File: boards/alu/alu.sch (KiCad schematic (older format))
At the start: 80 parts, among them U1 28C256, U2 74ACT08, U3 28C256, U4 74ACT00, U5 74ACT02

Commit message: PLCC-32 socket footprint
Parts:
- removed U1, U3: 28C256, Package_LCC:PLCC-28_SMD-Socket, symbol Memory_EEPROM:28C256
- added U1, U3: AT28C256-PLCC32, missing:PLCC-32_SMD_Socket, symbol missing:AT28C256-PLCC32
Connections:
- net GND: now also U1.16 (GND), U1.23 (~CE), U3.16 (GND), U3.23 (~CE)
- net VCC: now also U1.31 (~WE), U1.32 (VCC), U3.31 (~WE), U3.32 (VCC)
- net a0: now also U1.11 (A0)
- net a1: now also U1.10 (A1)
- net a2: now also U1.9 (A2)
- net a3: now also U1.8 (A3)
- net a4: now also U3.11 (A0)
- net a5: now also U3.10 (A1)
- net a6: now also U3.9 (A2)
- net a7: now also U3.8 (A3)
- net b0: now also U1.7 (A4)
- net b1: now also U1.6 (A5)
- net b2: now also U1.5 (A6)
- net b3: now also U1.4 (A7)
- net b4: now also U3.7 (A4)
- net b5: now also U3.6 (A5)
- net b6: now also U3.5 (A6)
- net b7: now also U3.4 (A7)
- net carry_in: now also U1.3 (A12), U3.3 (A12)
- net flags2: now also U3.18 (IO3)
- net flags3: now also U3.21 (IO6)
- net from_hi: now also U1.30 (A13)
- net from_lo: now also U3.30 (A13)
- net invert: now also U1.2 (A14), U3.2 (A14)
- net op0: now also U1.29 (A8), U3.29 (A8)
- net op1: now also U1.28 (A9), U3.28 (A9)
- net op2: now also U1.24 (A10), U3.24 (A10)
- net op3: now also U1.27 (A11), U3.27 (A11)
- net r0: now also U1.13 (IO0)
- net r1: now also U1.14 (IO1)
- net r2: now also U1.15 (IO2)
- net r3: now also U1.18 (IO3)
- net r4: now also U3.13 (IO0)
- net r5: now also U3.14 (IO1)
- net r6: now also U3.15 (IO2)
- net to_hi: now also U1.20 (IO5)
- net to_lo: now also U3.20 (IO5)
- net ~carry_hi: now also U3.19 (IO4)
- net ~carry_lo: now also U1.19 (IO4)
- net ~oe: now also U1.25 (~OE), U3.25 (~OE)
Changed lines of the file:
@@
 Comment4 ""
 $EndDescr
-$Comp
-L Memory_EEPROM:28C256 U1
-U 1 1 5FC22E82
-P 6500 3650
-F 0 "U1" H 6900 2700 50  0000 C CNN
-F 1 "28C256" H 6850 2550 50  0000 C CNN
-F 2 "Package_LCC:PLCC-28_SMD-Socket" H 6500 3650 50  0001 C CNN
-F 3 "http://ww1.microchip.com/downloads/en/DeviceDoc/doc0006.pdf" H 6500 3650 50  0001 C CNN
-	1    6500 3650
-	1    0    0    -1
-$EndComp
 Text Label 6100 2750 2    50   ~ 0
 a0
@@
 Text Label 8700 3250 0    50   ~ 0
 to_lo
-$Comp
-L Memory_EEPROM:28C256 U3
-U 1 1 5FC23A8E
-P 8300 3650
-F 0 "U3" H 8700 2700 50  0000 C CNN
-F 1 "28C256" H 8700 2550 50  0000 C CNN
-F 2 "Package_LCC:PLCC-28_SMD-Socket" H 8300 3650 50  0001 C CNN
-F 3 "http://ww1.microchip.com/downloads/en/DeviceDoc/doc0006.pdf" H 8300 3650 50  0001 C CNN
-	1    8300 3650
-	1    0    0    -1
-$EndComp
 NoConn ~ 8700 3450
 $Comp
@@
 L power:VCC #PWR01
 U 1 1 5FC2D9E5
-P 6100 4350
-F 0 "#PWR01" H 6100 4200 50  0001 C CNN
-F 1 "VCC" V 6118 4477 50  0000 L CNN
-F 2 "" H 6100 4350 50  0001 C CNN
-F 3 "" H 6100 4350 50  0001 C CNN
-	1    6100 4350
+P 6100 4450
+F 0 "#PWR01" H 6100 4300 50  0001 C CNN
+F 1 "VCC" V 6118 4577 50  0000 L CNN
+F 2 "" H 6100 4450 50  0001 C CNN
+F 3 "" H 6100 4450 50  0001 C CNN
+	1    6100 4450
 	0    -1   -1   0
 $EndComp
@@
 L power:VCC #PWR07
 U 1 1 5FC2E2AC
-P 7900 4350
-F 0 "#PWR07" H 7900 4200 50  0001 C CNN
-F 1 "VCC" V 7918 4477 50  0000 L CNN
-F 2 "" H 7900 4350 50  0001 C CNN
-F 3 "" H 7900 4350 50  0001 C CNN
-	1    7900 4350
+P 7900 4450
+F 0 "#PWR07" H 7900 4300 50  0001 C CNN
+F 1 "VCC" V 7918 4577 50  0000 L CNN
+F 2 "" H 7900 4450 50  0001 C CNN
+F 3 "" H 7900 4450 50  0001 C CNN
+	1    7900 4450
 	0    -1   -1   0
 $EndComp
@@
 Text Label 12950 3100 0    50   ~ 0
 flags[0..3]
-Text Label 7900 4450 2    50   ~ 0
+Text Label 7900 4350 2    50   ~ 0
 ~oe
-Text Label 6100 4450 2    50   ~ 0
+Text Label 6100 4350 2    50   ~ 0
 ~oe
 Text Label 9350 3650 0    50   ~ 0
@@
 Wire Bus Line
 	10750 1700 10750 3100
+$Comp
+L missing:AT28C256-PLCC32 U1
+U 1 1 60197966
+P 6500 3650
+F 0 "U1" H 6500 4931 50  0000 C CNN
+F 1 "AT28C256-PLCC32" H 6500 4840 50  0000 C CNN
+F 2 "missing:PLCC-32_SMD_Socket" H 6750 4000 50  0001 C CNN
+F 3 "http://ww1.microchip.com/downloads/en/DeviceDoc/doc0006.pdf" H 6750 4000 50  0001 C CNN
+	1    6500 3650
+	1    0    0    -1
+$EndComp
+$Comp
+L missing:AT28C256-PLCC32 U3
+U 1 1 60199147
+P 8300 3650
+F 0 "U3" H 8300 4931 50  0000 C CNN
+F 1 "AT28C256-PLCC32" H 8300 4840 50  0000 C CNN
+F 2 "missing:PLCC-32_SMD_Socket" H 8550 4000 50  0001 C CNN
+F 3 "http://ww1.microchip.com/downloads/en/DeviceDoc/doc0006.pdf" H 8550 4000 50  0001 C CNN
+	1    8300 3650
+	1    0    0    -1
+$EndComp
 $EndSCHEMATC

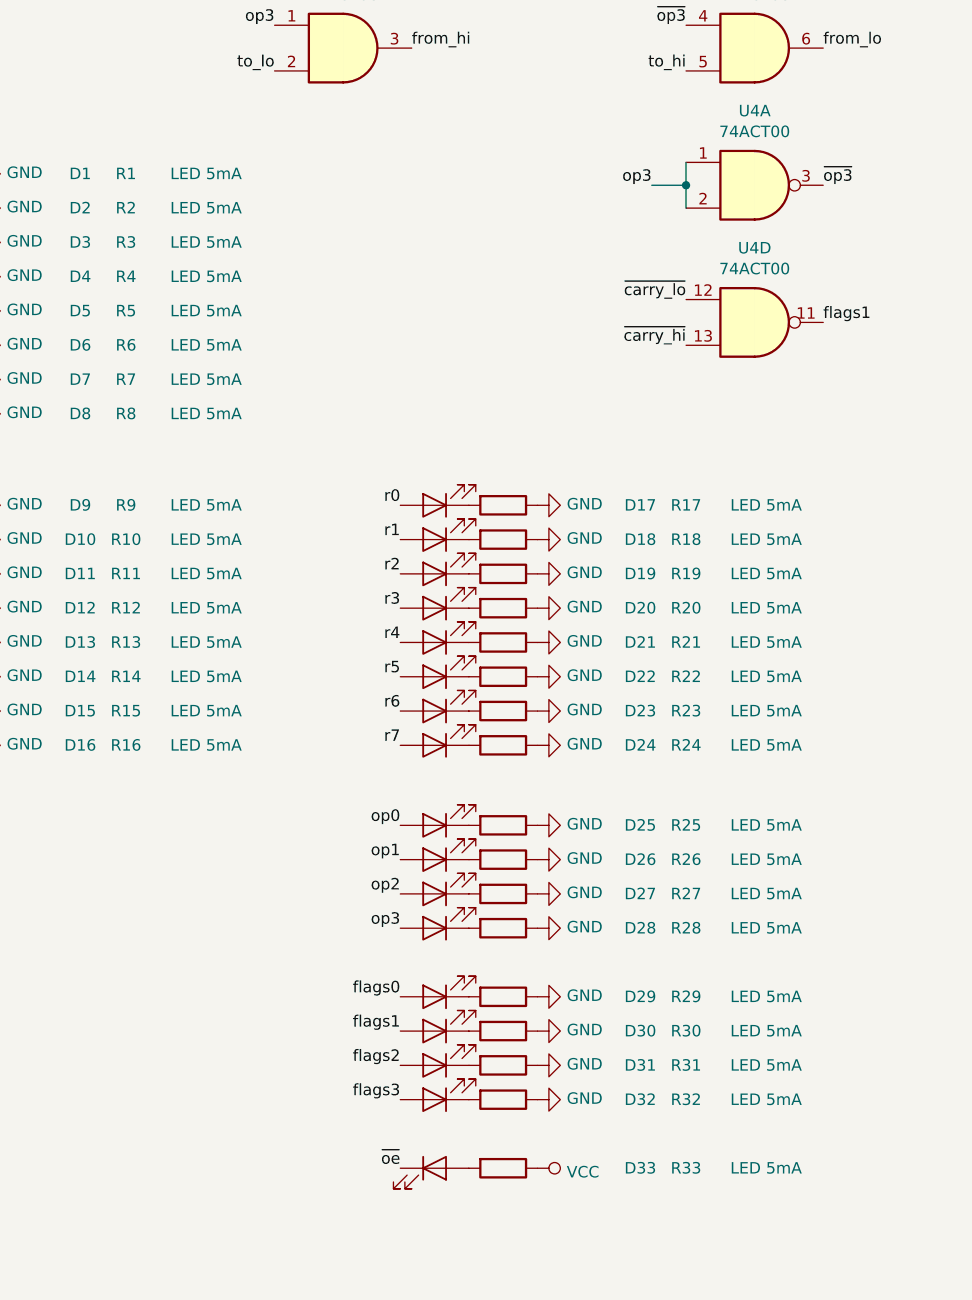
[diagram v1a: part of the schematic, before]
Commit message: LEDs and LED resistors
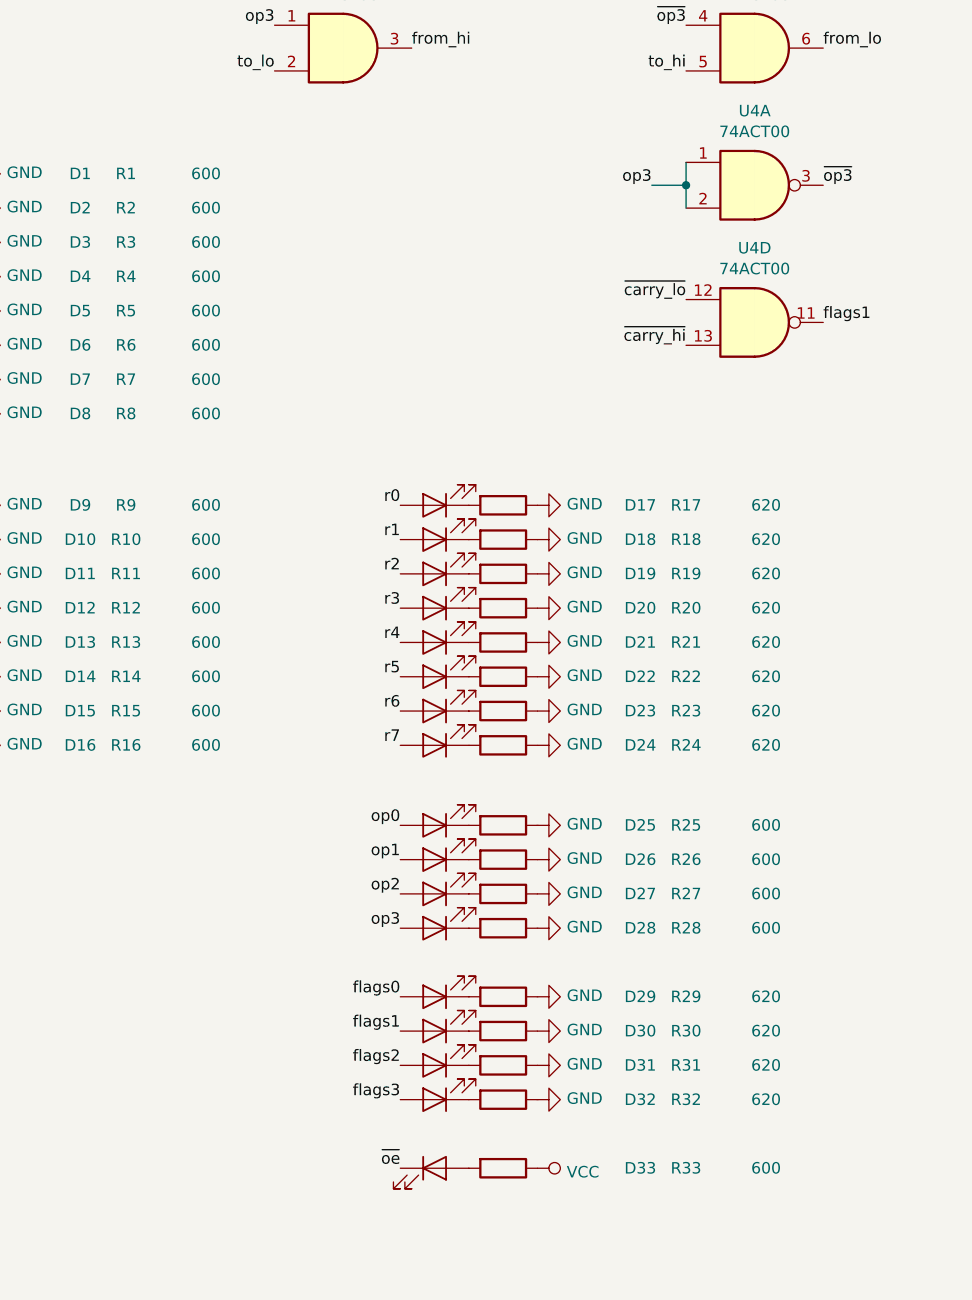
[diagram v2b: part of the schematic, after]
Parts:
- D1, D10, D11, D12, D13, D14, D15, D16, D2, D25, D26, D27, D28, D3, D33, D4, D5, D6, D7, D8, D9: value LED -> KP-2012CGCK
- D17, D18, D19, D20, D21, D22, D23, D24, D29, D30, D31, D32: value LED -> KP-2012EC
- R1, R10, R11, R12, R13, R14, R15, R16, R2, R25, R26, R27, R28, R3, R33, R4, R5, R6, R7, R8, R9: value LED 5mA -> 600
- R17, R18, R19, R20, R21, R22, R23, R24, R29, R30, R31, R32: value LED 5mA -> 620

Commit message: Part names
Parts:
- U2: value 74ACT08 -> SN74ACT08PW
- U4: value 74ACT00 -> 74ACT00MTCX; footprint Package_SO:SOIC-14_3.9x8.7mm_P1.27mm -> Package_SO:TSSOP-14_4.4x5mm_P0.65mm
- U5: value 74ACT02 -> MC74ACT02DTR2G
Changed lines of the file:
@@
 P 6500 5500
 F 0 "U2" H 6500 5825 50  0000 C CNN
-F 1 "74ACT08" H 6500 5734 50  0000 C CNN
+F 1 "SN74ACT08PW" H 6500 5734 50  0000 C CNN
 F 2 "Package_SO:TSSOP-14_4.4x5mm_P0.65mm" H 6500 5500 50  0001 C CNN
 F 3 "http://www.ti.com/lit/gpn/sn74LS08" H 6500 5500 50  0001 C CNN
@@
 P 8300 5500
 F 0 "U2" H 8300 5825 50  0000 C CNN
-F 1 "74ACT08" H 8300 5734 50  0000 C CNN
+F 1 "SN74ACT08PW" H 8300 5734 50  0000 C CNN
 F 2 "Package_SO:TSSOP-14_4.4x5mm_P0.65mm" H 8300 5500 50  0001 C CNN
 F 3 "http://www.ti.com/lit/gpn/sn74LS08" H 8300 5500 50  0001 C CNN
@@
 P 10100 5750
 F 0 "U5" H 10100 6075 50  0000 C CNN
-F 1 "74ACT02" H 10100 5984 50  0000 C CNN
+F 1 "MC74ACT02DTR2G" H 10100 5984 50  0000 C CNN
 F 2 "Package_SO:TSSOP-14_4.4x5mm_P0.65mm" H 10100 5750 50  0001 C CNN
 F 3 "http://www.ti.com/lit/gpn/sn74ls02" H 10100 5750 50  0001 C CNN
@@
 P 10100 6300
 F 0 "U5" H 10100 6625 50  0000 C CNN
-F 1 "74ACT02" H 10100 6534 50  0000 C CNN
+F 1 "MC74ACT02DTR2G" H 10100 6534 50  0000 C CNN
 F 2 "Package_SO:TSSOP-14_4.4x5mm_P0.65mm" H 10100 6300 50  0001 C CNN
 F 3 "http://www.ti.com/lit/gpn/sn74ls02" H 10100 6300 50  0001 C CNN
@@
 P 10100 6850
 F 0 "U5" H 10100 7175 50  0000 C CNN
-F 1 "74ACT02" H 10100 7084 50  0000 C CNN
+F 1 "MC74ACT02DTR2G" H 10100 7084 50  0000 C CNN
 F 2 "Package_SO:TSSOP-14_4.4x5mm_P0.65mm" H 10100 6850 50  0001 C CNN
 F 3 "http://www.ti.com/lit/gpn/sn74ls02" H 10100 6850 50  0001 C CNN
@@
 P 10100 7400
 F 0 "U5" H 10100 7725 50  0000 C CNN
-F 1 "74ACT02" H 10100 7634 50  0000 C CNN
+F 1 "MC74ACT02DTR2G" H 10100 7634 50  0000 C CNN
 F 2 "Package_SO:TSSOP-14_4.4x5mm_P0.65mm" H 10100 7400 50  0001 C CNN
 F 3 "http://www.ti.com/lit/gpn/sn74ls02" H 10100 7400 50  0001 C CNN
@@
 P 11050 6050
 F 0 "U2" H 11050 6375 50  0000 C CNN
-F 1 "74ACT08" H 11050 6284 50  0000 C CNN
+F 1 "SN74ACT08PW" H 11050 6284 50  0000 C CNN
 F 2 "Package_SO:TSSOP-14_4.4x5mm_P0.65mm" H 11050 6050 50  0001 C CNN
 F 3 "http://www.ti.com/lit/gpn/sn74LS08" H 11050 6050 50  0001 C CNN
@@
 P 11050 7100
 F 0 "U2" H 11050 7425 50  0000 C CNN
-F 1 "74ACT08" H 11050 7334 50  0000 C CNN
+F 1 "SN74ACT08PW" H 11050 7334 50  0000 C CNN
 F 2 "Package_SO:TSSOP-14_4.4x5mm_P0.65mm" H 11050 7100 50  0001 C CNN
 F 3 "http://www.ti.com/lit/gpn/sn74LS08" H 11050 7100 50  0001 C CNN
@@
 P 13500 8900
 F 0 "U2" H 13730 8946 50  0000 L CNN
-F 1 "74ACT08" H 13730 8855 50  0000 L CNN
+F 1 "SN74ACT08PW" H 13730 8855 50  0000 L CNN
 F 2 "Package_SO:TSSOP-14_4.4x5mm_P0.65mm" H 13500 8900 50  0001 C CNN
 F 3 "http://www.ti.com/lit/gpn/sn74LS08" H 13500 8900 50  0001 C CNN
@@
 P 14350 8900
 F 0 "U5" H 14580 8946 50  0000 L CNN
-F 1 "74ACT02" H 14580 8855 50  0000 L CNN
+F 1 "MC74ACT02DTR2G" H 14580 8855 50  0000 L CNN
 F 2 "Package_SO:TSSOP-14_4.4x5mm_P0.65mm" H 14350 8900 50  0001 C CNN
 F 3 "http://www.ti.com/lit/gpn/sn74ls02" H 14350 8900 50  0001 C CNN
@@
 P 8300 6100
 F 0 "U4" H 8300 6425 50  0000 C CNN
-F 1 "74ACT00" H 8300 6334 50  0000 C CNN
-F 2 "Package_SO:SOIC-14_3.9x8.7mm_P1.27mm" H 8300 6100 50  0001 C CNN
+F 1 "74ACT00MTCX" H 8300 6334 50  0000 C CNN
+F 2 "Package_SO:TSSOP-14_4.4x5mm_P0.65mm" H 8300 6100 50  0001 C CNN
 F 3 "http://www.ti.com/lit/gpn/sn74hc00" H 8300 6100 50  0001 C CNN
 	1    8300 6100
@@
 P 11900 6550
 F 0 "U4" H 11900 6875 50  0000 C CNN
-F 1 "74ACT00" H 11900 6784 50  0000 C CNN
-F 2 "Package_SO:SOIC-14_3.9x8.7mm_P1.27mm" H 11900 6550 50  0001 C CNN
+F 1 "74ACT00MTCX" H 11900 6784 50  0000 C CNN
+F 2 "Package_SO:TSSOP-14_4.4x5mm_P0.65mm" H 11900 6550 50  0001 C CNN
 F 3 "http://www.ti.com/lit/gpn/sn74hc00" H 11900 6550 50  0001 C CNN
 	2    11900 6550
@@
 P 12750 6550
 F 0 "U4" H 12750 6875 50  0000 C CNN
-F 1 "74ACT00" H 12750 6784 50  0000 C CNN
-F 2 "Package_SO:SOIC-14_3.9x8.7mm_P1.27mm" H 12750 6550 50  0001 C CNN
+F 1 "74ACT00MTCX" H 12750 6784 50  0000 C CNN
+F 2 "Package_SO:TSSOP-14_4.4x5mm_P0.65mm" H 12750 6550 50  0001 C CNN
 F 3 "http://www.ti.com/lit/gpn/sn74hc00" H 12750 6550 50  0001 C CNN
 	3    12750 6550
@@
 P 8300 6700
 F 0 "U4" H 8300 7025 50  0000 C CNN
-F 1 "74ACT00" H 8300 6934 50  0000 C CNN
-F 2 "Package_SO:SOIC-14_3.9x8.7mm_P1.27mm" H 8300 6700 50  0001 C CNN
+F 1 "74ACT00MTCX" H 8300 6934 50  0000 C CNN
+F 2 "Package_SO:TSSOP-14_4.4x5mm_P0.65mm" H 8300 6700 50  0001 C CNN
 F 3 "http://www.ti.com/lit/gpn/sn74hc00" H 8300 6700 50  0001 C CNN
 	4    8300 6700
@@
 P 15250 8900
 F 0 "U4" H 15480 8946 50  0000 L CNN
-F 1 "74ACT00" H 15480 8855 50  0000 L CNN
-F 2 "Package_SO:SOIC-14_3.9x8.7mm_P1.27mm" H 15250 8900 50  0001 C CNN
+F 1 "74ACT00MTCX" H 15480 8855 50  0000 L CNN
+F 2 "Package_SO:TSSOP-14_4.4x5mm_P0.65mm" H 15250 8900 50  0001 C CNN
 F 3 "http://www.ti.com/lit/gpn/sn74hc00" H 15250 8900 50  0001 C CNN
 	5    15250 8900
